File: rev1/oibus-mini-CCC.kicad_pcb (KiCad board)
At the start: 2 copper layers, 37 x 60 mm, 85 parts, among them J1 Conn_01x04_Female, J2 USB_B_Micro, J3 uavcan_5pins, J4 Conn_01x02_Female, P1 TC2030-MCP, Q1 DMG3415U-7, Q2 NMOS, Q3 NMOS, SW1 SW_Push, U1 AP2112K-3.3, U10 TPD3E001DRLR, U2 SAM-M8Q, U3 NINA-B311-00B, U4 MCP73831-2-OT, U5 MCP1624T, U6 SHT31-DIS-B, U7 TCAN330, U8 STM32F303CCTx, U9 DW01C-G, Y1 16M, Y2 32kHz

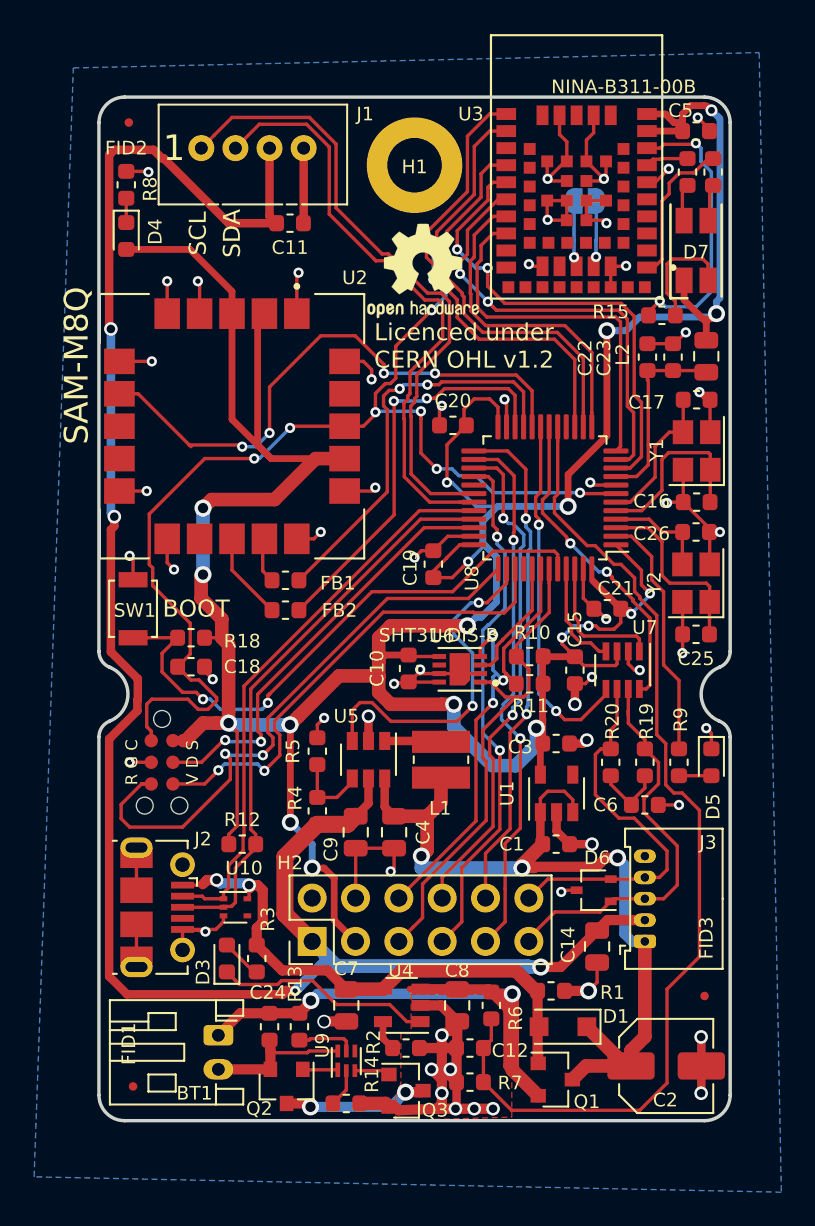
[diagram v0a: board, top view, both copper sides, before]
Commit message: moved the grove connector inside
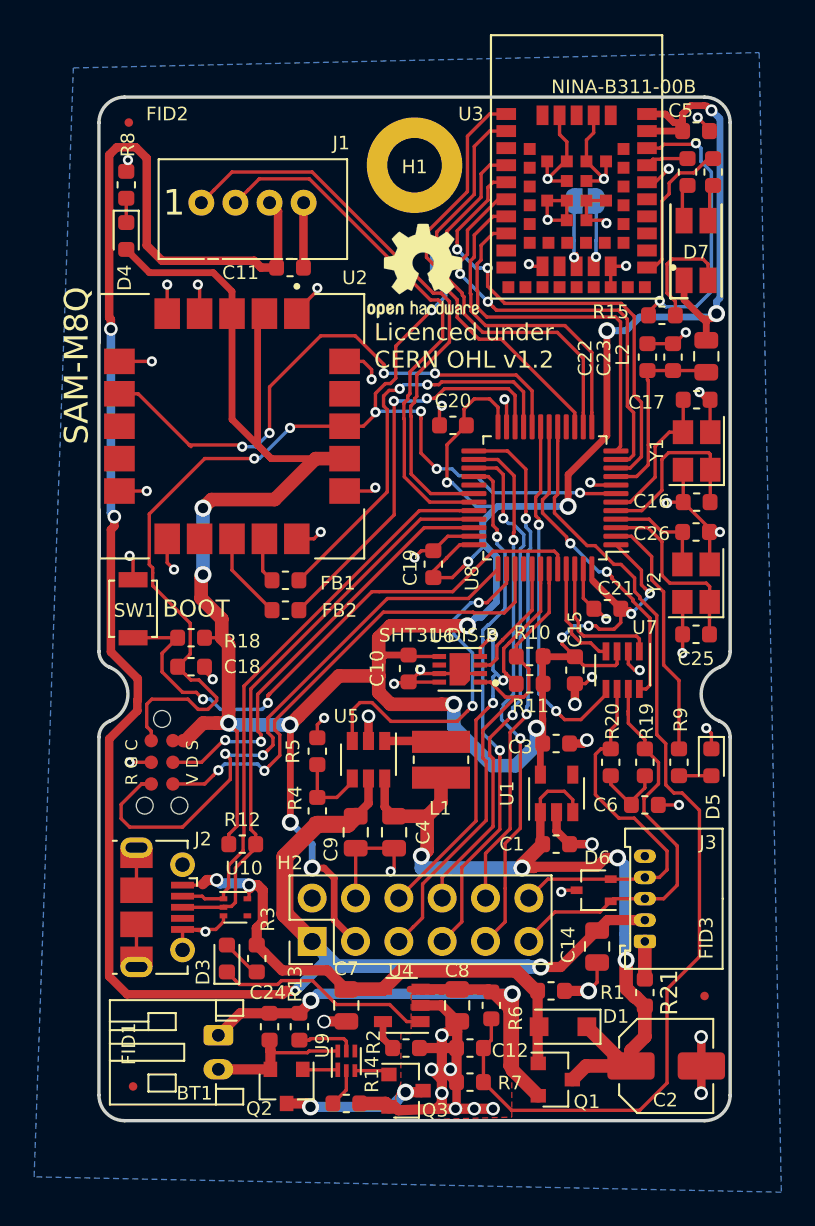
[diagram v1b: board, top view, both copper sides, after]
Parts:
- added R21: DNP, Resistor_SMD:R_0603_1608Metric, F.Cu at (32.0, -7.50)
- moved J1 3.20 mm to (6.00, -53.8)
- moved C11 2.60 mm to (11.2, -50.0)
- renumbered J4 to NFC
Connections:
- J3 pad 1: /VIN -> Net-(J3-Pad1)
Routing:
- net SPS_TX: track 35.3 -> 31.5 mm
- net +5V: track 114.9 -> 118.5 mm
- net SPS_RX: track 37.2 -> 33.7 mm
- net Net-(J3-Pad1): track 0.00 -> 2.21 mm
- net GND: track 154.2 -> 152.2 mm
- net NINA_DSR: track 25.6 -> 23.9 mm
- net /VIN: track 50.5 -> 50.1 mm, vias 3 -> 4
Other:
- board text added: "<MCU"
- board text added: ">MCU"
- board text added: "Alt:"
- board text removed: "<<MCU >>MCU"
- board text removed: "SPS30"

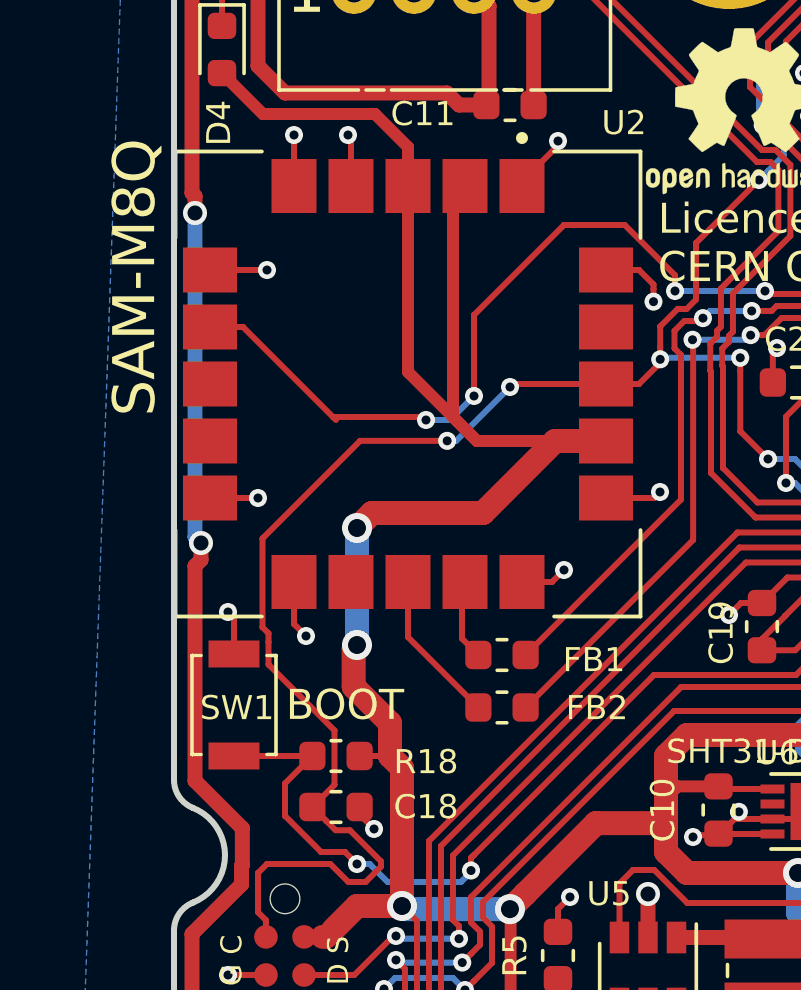
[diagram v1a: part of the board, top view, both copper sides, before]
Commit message: corrected the boot pin voltage level
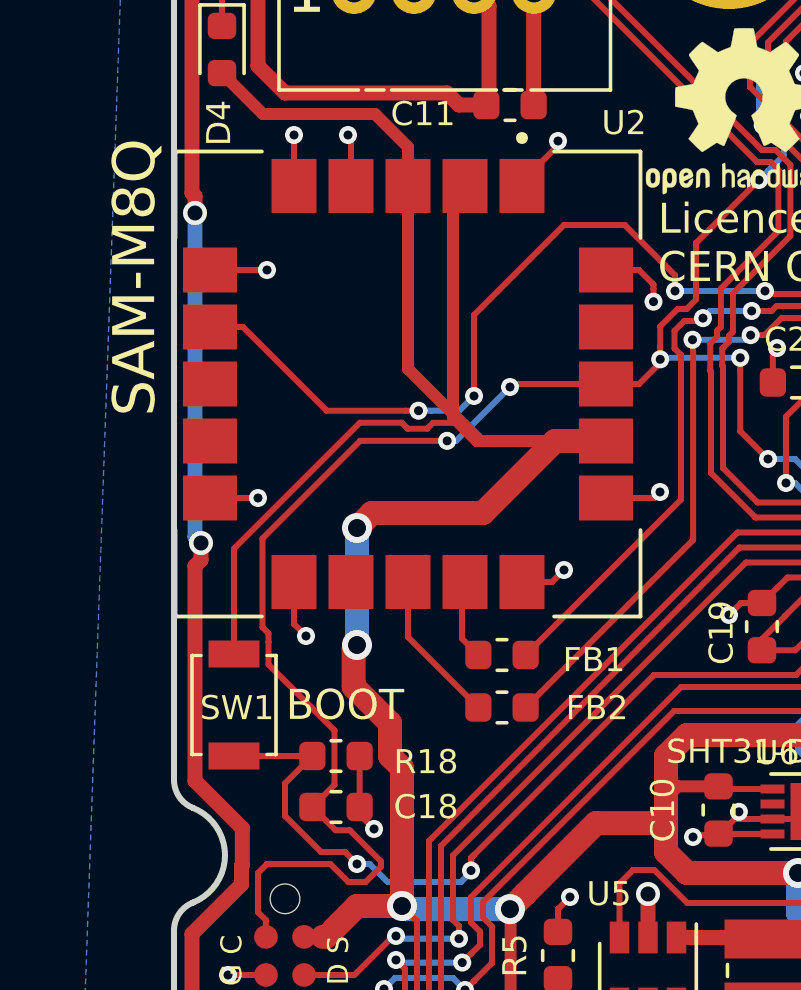
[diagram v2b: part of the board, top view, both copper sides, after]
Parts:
- C2: value 47u 35V -> 47u 16V
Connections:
- R18 pad 2: +3V3 -> GND
- SW1 pad 2: GND -> +3V3
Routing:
- net +3V3: track 219.8 -> 232.0 mm
- net GND: track 152.2 -> 152.4 mm, vias 56 -> 55
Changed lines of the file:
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@@
     (thickness 1.6)
     (drawings 35)
-    (tracks 1359)
+    (tracks 1367)
     (zones 0)
     (modules 86)
@@
       (effects (font (size 0.8 0.8) (thickness 0.15)))
     )
-    (fp_text value "47u 35V" (at 0 3.7) (layer F.Fab)
+    (fp_text value "47u 16V" (at 0 3.7) (layer F.Fab)
       (effects (font (size 1 1) (thickness 0.15)))
     )
@@
       (net 66 /BOOT))
     (pad 2 smd rect (at 1.7 0 90) (size 0.9 1.7) (layers F.Cu F.Paste F.Mask)
-      (net 2 GND))
+      (net 3 +3V3))
     (model ${KISYS3DMOD}/Button_Switch_SMD.3dshapes/SW_SPST_B3U-1000P.wrl
       (at (xyz 0 0 0))
@@
       (net 66 /BOOT))
     (pad 2 smd roundrect (at 0.7875 0) (size 0.875 0.95) (layers F.Cu F.Paste F.Mask) (roundrect_rratio 0.25)
-      (net 3 +3V3))
+      (net 2 GND))
     (model ${KISYS3DMOD}/Resistor_SMD.3dshapes/R_0603_1608Metric.wrl
       (at (xyz 0 0 0))
@@
   (segment (start 4 -34.1) (end 4 -32.7) (width 0.2) (layer F.Cu) (net 2))
   (segment (start 4.5 -32.2) (end 4.4 -32.3) (width 0.2) (layer F.Cu) (net 2))
-  (via (at 1.8 -33.1) (size 0.6) (drill 0.3) (layers F.Cu B.Cu) (net 2))
-  (segment (start 2 -32.9) (end 1.8 -33.1) (width 0.2) (layer F.Cu) (net 2))
-  (segment (start 2 -31.7) (end 2 -32.9) (width 0.2) (layer F.Cu) (net 2))
   (segment (start 15.05 -13.05) (end 15.04 -13.04) (width 0.2) (layer F.Cu) (net 2))
   (segment (start 15.05 -15.9625) (end 15.05 -13.05) (width 0.2) (layer F.Cu) (net 2))
@@
   (segment (start 11.9875 -53.7875) (end 12 -53.8) (width 0.5) (layer F.Cu) (net 2))
   (segment (start 11.9875 -50) (end 11.9875 -53.7875) (width 0.5) (layer F.Cu) (net 2))
+  (segment (start 6.1875 -28.3) (end 6.1875 -26.6) (width 0.2) (layer F.Cu) (net 2))
   (segment (start 30.269999 -26.669999) (end 28.417501 -26.669999) (width 0.2) (layer F.Cu) (net 3))
   (segment (start 30.37 -26.77) (end 30.269999 -26.669999) (width 0.2) (layer F.Cu) (net 3))
@@
   (segment (start 30.5875 -30) (end 28.941634 -31.645866) (width 0.4) (layer F.Cu) (net 3) (status 30))
   (via (at 21.6 -28.999979) (size 1) (drill 0.6) (layers F.Cu B.Cu) (net 3))
-  (segment (start 7.8 -47.3) (end 7.8 -41.1) (width 0.4) (layer F.Cu) (net 3) (status 10))
   (segment (start 10.1 -38.8) (end 14.4 -38.8) (width 0.4) (layer F.Cu) (net 3) (status 20))
-  (segment (start 7.8 -41.1) (end 10.1 -38.8) (width 0.4) (layer F.Cu) (net 3))
   (via (at 25.639663 -22.999179) (size 1) (drill 0.6) (layers F.Cu B.Cu) (net 3))
   (segment (start 26.0125 -23.372016) (end 25.639663 -22.999179) (width 0.4) (layer F.Cu) (net 3))
@@
   (segment (start 20.4 -39.6125) (end 21.5375 -40.75) (width 0.2) (layer F.Cu) (net 3))
   (segment (start 20.4 -37.4) (end 20.4 -39.6125) (width 0.2) (layer F.Cu) (net 3))
-  (segment (start 9.3 -39.6) (end 10.1 -38.8) (width 0.4) (layer F.Cu) (net 3))
   (segment (start 9.3 -46.9) (end 9.3 -39.6) (width 0.4) (layer F.Cu) (net 3))
   (segment (start 9.7 -47.3) (end 9.3 -46.9) (width 0.4) (layer F.Cu) (net 3))
@@
   (segment (start 36 -47.1) (end 31.7 -47.1) (width 0.4) (layer B.Cu) (net 3))
   (segment (start 36.2 -47.3) (end 36 -47.1) (width 0.4) (layer B.Cu) (net 3))
-  (segment (start 6.1875 -28.3) (end 7.2 -28.3) (width 0.2) (layer F.Cu) (net 3))
   (segment (start 5.989176 -31.889176) (end 6.1 -32) (width 0.8) (layer F.Cu) (net 3))
   (segment (start 5.989176 -30.610824) (end 5.989176 -31.889176) (width 0.8) (layer F.Cu) (net 3))
@@
   (segment (start 1.6 -51.0625) (end 2.9625 -49.7) (width 0.4) (layer F.Cu) (net 3))
   (segment (start 2.9625 -49.7) (end 6.7 -49.7) (width 0.4) (layer F.Cu) (net 3))
+  (segment (start 10.1 -38.906004) (end 10.1 -38.8) (width 0.4) (layer F.Cu) (net 3))
+  (segment (start 7.8 -47.3) (end 7.8 -41.206004) (width 0.4) (layer F.Cu) (net 3))
+  (segment (start 7.8 -41.206004) (end 10.1 -38.906004) (width 0.4) (layer F.Cu) (net 3))
+  (segment (start 7.790001 -39.209999) (end 7.59001 -39.40999) (width 0.2) (layer F.Cu) (net 3))
+  (segment (start 8.438001 -39.209999) (end 7.790001 -39.209999) (width 0.2) (layer F.Cu) (net 3))
+  (segment (start 8.633028 -39.405026) (end 8.438001 -39.209999) (width 0.2) (layer F.Cu) (net 3))
+  (segment (start 9.3 -39.6) (end 9.68 -39.22) (width 0.4) (layer F.Cu) (net 3))
+  (segment (start 9.494974 -39.405026) (end 8.633028 -39.405026) (width 0.2) (layer F.Cu) (net 3))
+  (segment (start 9.68 -39.22) (end 9.494974 -39.405026) (width 0.2) (layer F.Cu) (net 3))
+  (segment (start 9.68 -39.22) (end 10.1 -38.8) (width 0.4) (layer F.Cu) (net 3))
+  (segment (start 2 -32.35) (end 2 -31.7) (width 0.2) (layer F.Cu) (net 3))
+  (segment (start 2 -35.211998) (end 2 -32.35) (width 0.2) (layer F.Cu) (net 3))
+  (segment (start 6.197992 -39.40999) (end 2 -35.211998) (width 0.2) (layer F.Cu) (net 3))
+  (segment (start 7.59001 -39.40999) (end 6.197992 -39.40999) (width 0.2) (layer F.Cu) (net 3))
   (segment (start 26.391624 -36.775628) (end 25.999998 -36.384002) (width 0.2) (layer F.Cu) (net 4))
   (segment (start 25.999998 -36.384002) (end 25.999998 -35.615998) (width 0.2) (layer F.Cu) (net 4))
@@
   (segment (start 32.474999 -56.349999) (end 32.940001 -56.349999) (width 0.2) (layer F.Cu) (net 56) (status 10))
   (segment (start 32.125 -56) (end 32.474999 -56.349999) (width 0.2) (layer F.Cu) (net 56) (status 30))
-  (segment (start 1.2 -42.6) (end 2.3 -42.6) (width 0.2) (layer F.Cu) (net 57))
-  (segment (start 5.3 -39.6) (end 8.3 -39.6) (width 0.2) (layer F.Cu) (net 57))
-  (segment (start 2.3 -42.6) (end 5.3 -39.6) (width 0.2) (layer F.Cu) (net 57))
-  (via (at 8.4 -39.5) (size 0.6) (drill 0.3) (layers F.Cu B.Cu) (net 57))
-  (segment (start 8.3 -39.6) (end 8.4 -39.5) (width 0.2) (layer F.Cu) (net 57))
-  (segment (start 5.3 -39.6) (end 5.4 -39.5) (width 0.2) (layer F.Cu) (net 57))
-  (segment (start 9.2 -39.5) (end 10 -40.3) (width 0.2) (layer B.Cu) (net 57))
   (via (at 10 -40.3) (size 0.6) (drill 0.3) (layers F.Cu B.Cu) (net 57))
-  (segment (start 8.4 -39.5) (end 9.2 -39.5) (width 0.2) (layer B.Cu) (net 57))
   (via (at 19.7 -43.8) (size 0.6) (drill 0.3) (layers F.Cu B.Cu) (net 57))
   (segment (start 25.391624 -42.774074) (end 24.465698 -43.7) (width 0.2) (layer F.Cu) (net 57))
@@
   (segment (start 16.7 -44.224264) (end 16.7 -43.8) (width 0.2) (layer F.Cu) (net 57))
   (segment (start 10 -40.3) (end 10 -43) (width 0.2) (layer F.Cu) (net 57))
+  (via (at 8.15 -39.81) (size 0.6) (drill 0.3) (layers F.Cu B.Cu) (net 57))
+  (segment (start 8.574264 -39.81) (end 8.15 -39.81) (width 0.2) (layer B.Cu) (net 57))
+  (segment (start 10 -40.3) (end 9.51 -39.81) (width 0.2) (layer B.Cu) (net 57))
+  (segment (start 9.51 -39.81) (end 8.574264 -39.81) (width 0.2) (layer B.Cu) (net 57))
+  (segment (start 7.725736 -39.81) (end 8.15 -39.81) (width 0.2) (layer F.Cu) (net 57))
+  (segment (start 5.09 -39.81) (end 7.725736 -39.81) (width 0.2) (layer F.Cu) (net 57))
+  (segment (start 2.3 -42.6) (end 5.09 -39.81) (width 0.2) (layer F.Cu) (net 57))
+  (segment (start 1.2 -42.6) (end 2.3 -42.6) (width 0.2) (layer F.Cu) (net 57))
   (segment (start 21.300037 -48.385067) (end 21.400035 -48.285069) (width 0.2) (layer F.Cu) (net 58))
   (segment (start 21.400035 -47.299965) (end 22.499989 -46.200011) (width 0.2) (layer F.Cu) (net 58))
